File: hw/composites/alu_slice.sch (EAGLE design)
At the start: 8 parts, among them CON2 GENERIC-2X10

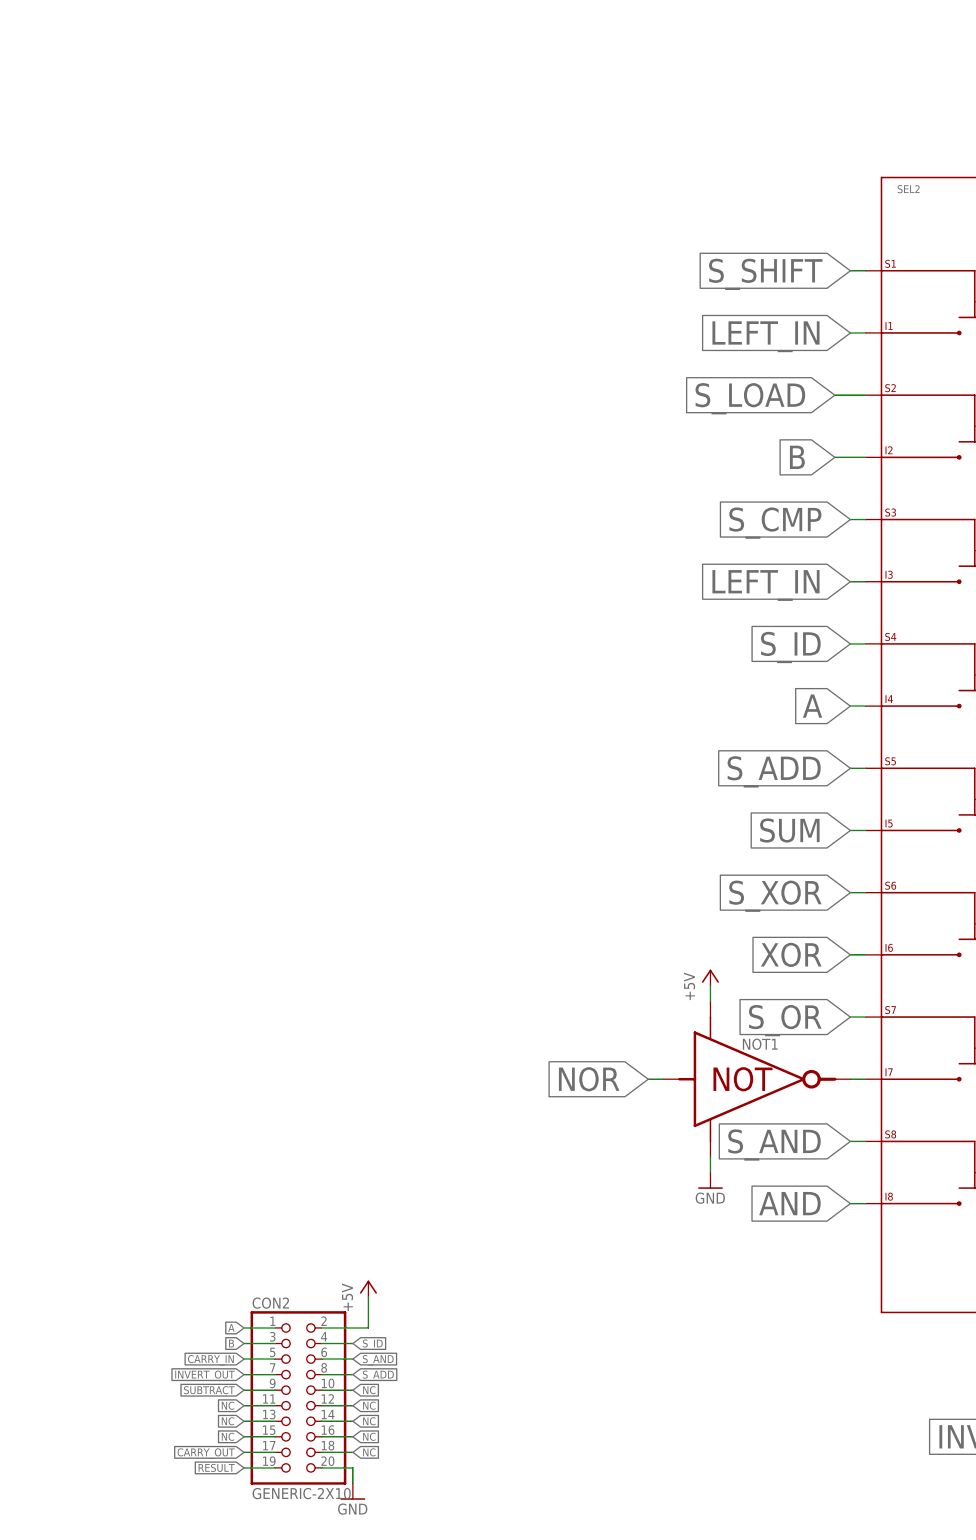
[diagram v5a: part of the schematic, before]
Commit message: adds support for bit shifts
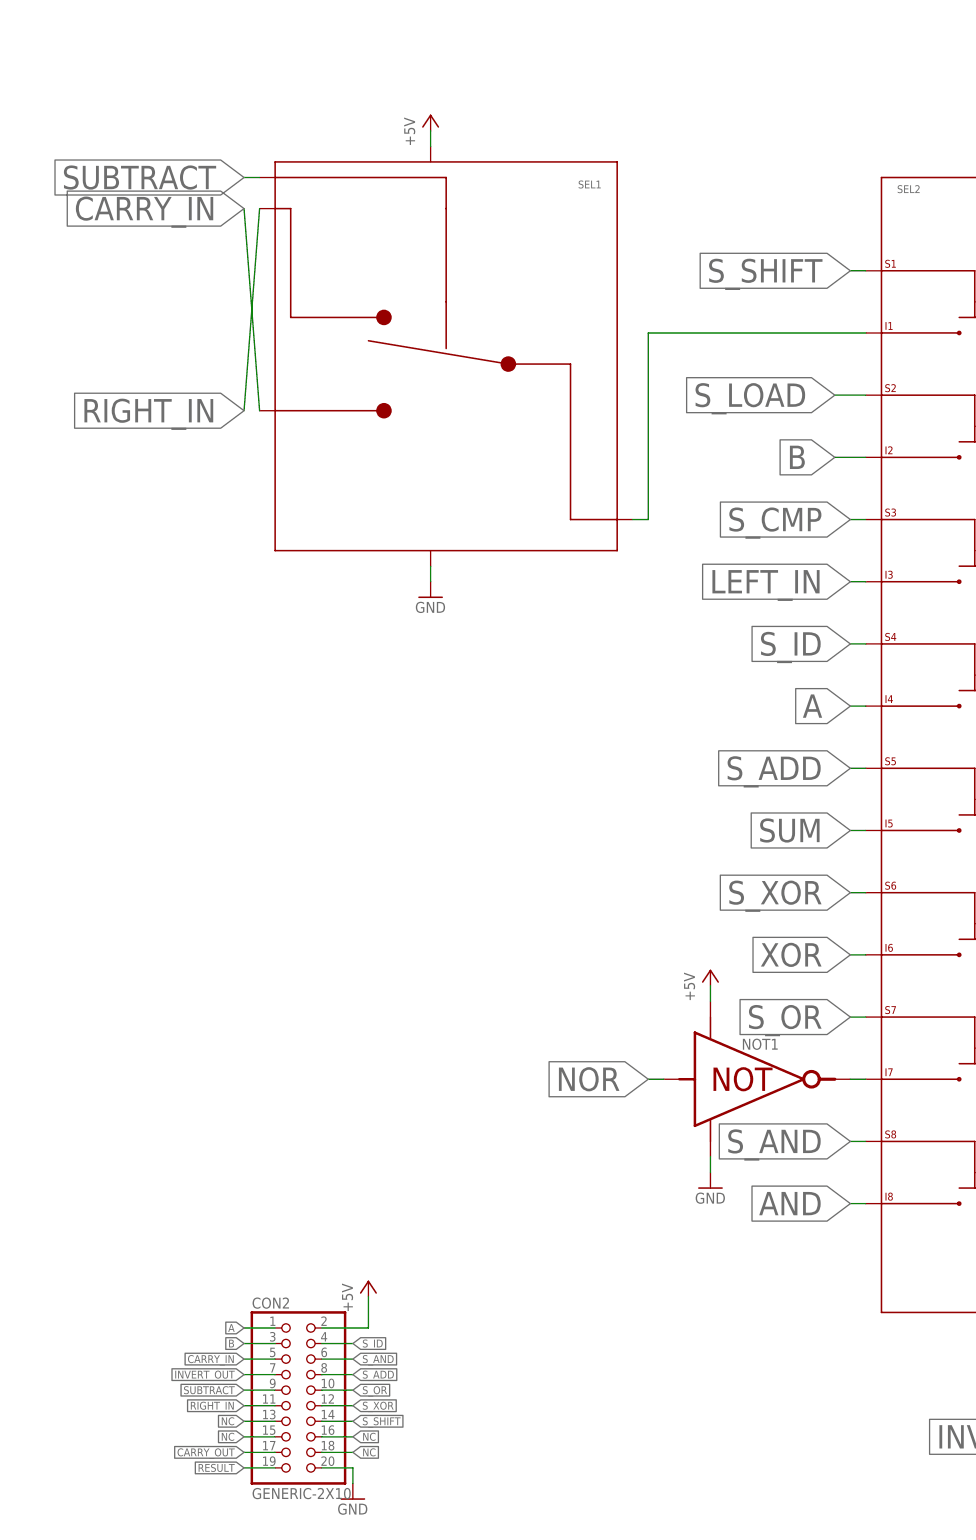
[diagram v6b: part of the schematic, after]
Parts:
- added SEL1: 1_BIT_SELECT, p.peter-gator:1_BIT_SELECT
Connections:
- new net N$5: SEL1.OUT, SEL2.I1
- new net RIGHT_IN: CON2.11, SEL1.A
- net +5V: now also SEL1._VP
- net CARRY_IN: now also SEL1.B
- net GND: now also SEL1._VN
- net LEFT_IN: no longer SEL2.I1
- net NC: no longer CON2.10, CON2.11, CON2.12, CON2.14
- net SUBTRACT: now also SEL1.SEL
- net S_OR: now also CON2.10
- net S_SHIFT: now also CON2.14
- net S_XOR: now also CON2.12
